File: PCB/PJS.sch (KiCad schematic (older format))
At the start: 40 parts, among them J1 HFW8R-1STE1H1LF_FFC, K1 G2R-2-DC5_Relay, Q1 MMBT222A_Transistor, X1 XT30-F_MotorConnector, X2 XT30-F_MotorConnector, X3 XT60-F_BatteryConnector

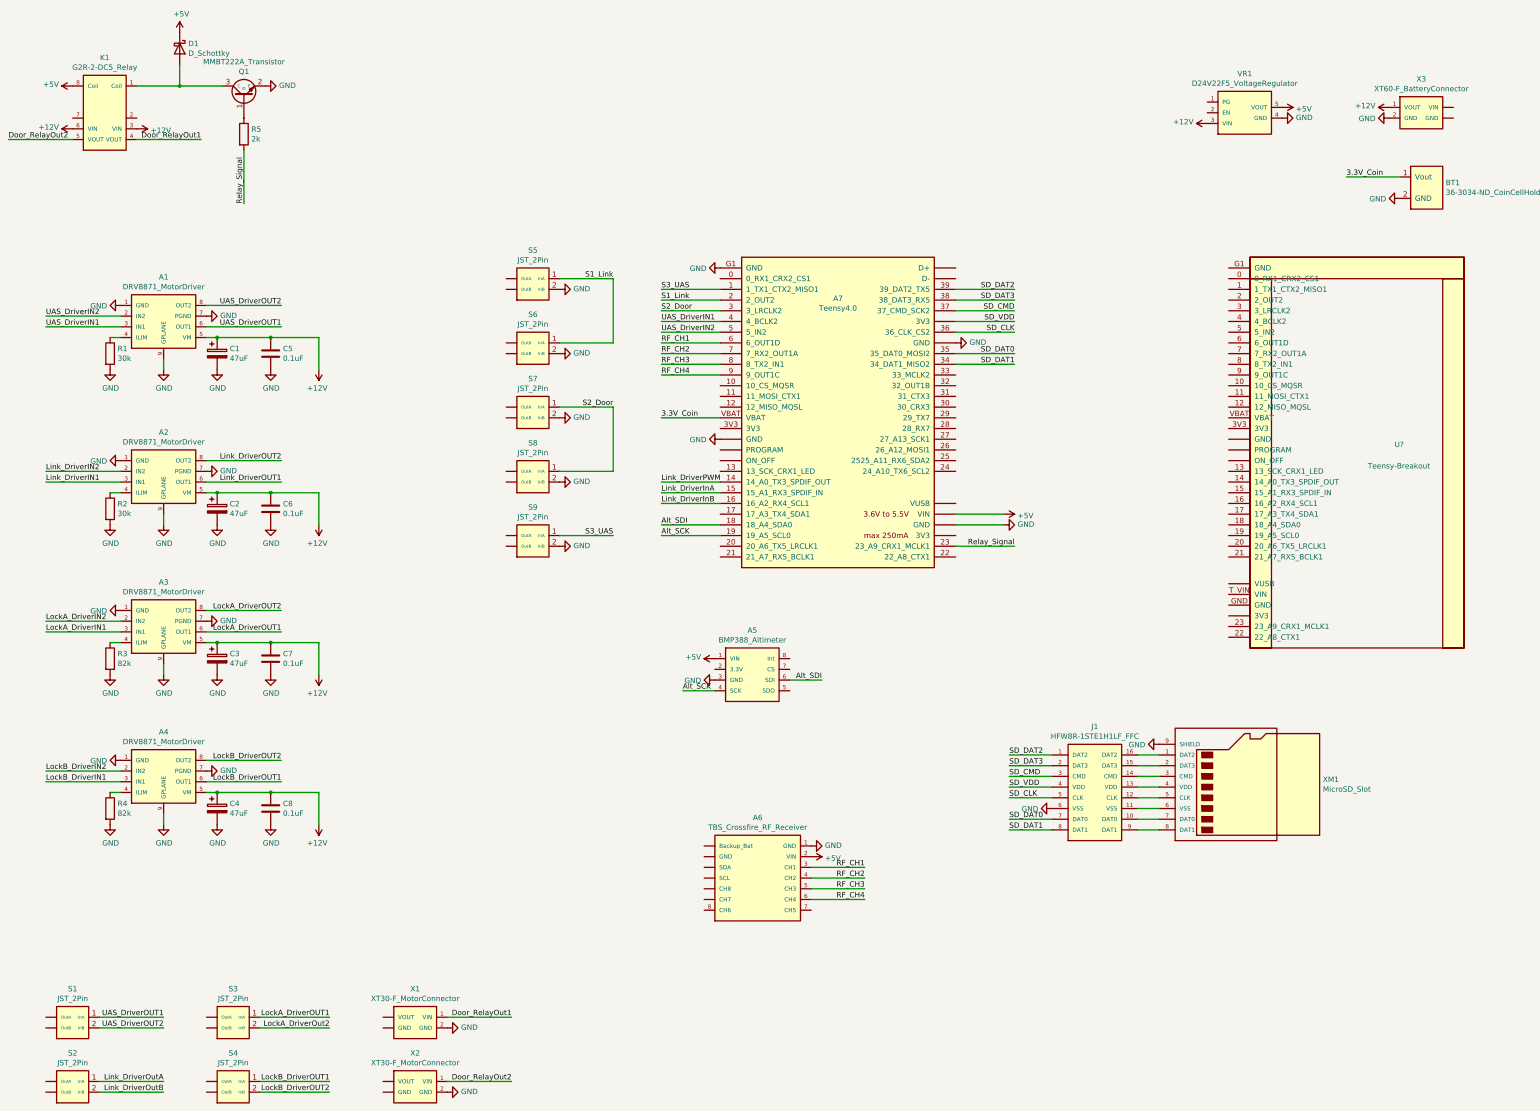
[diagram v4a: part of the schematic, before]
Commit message: 99.5% Complete Schematic and Footprint
The only item missing is the footprint for the RF receiver, which is now being mounted on the board.

Connectors for the motors and switches have now changed to two different locking JSTS.
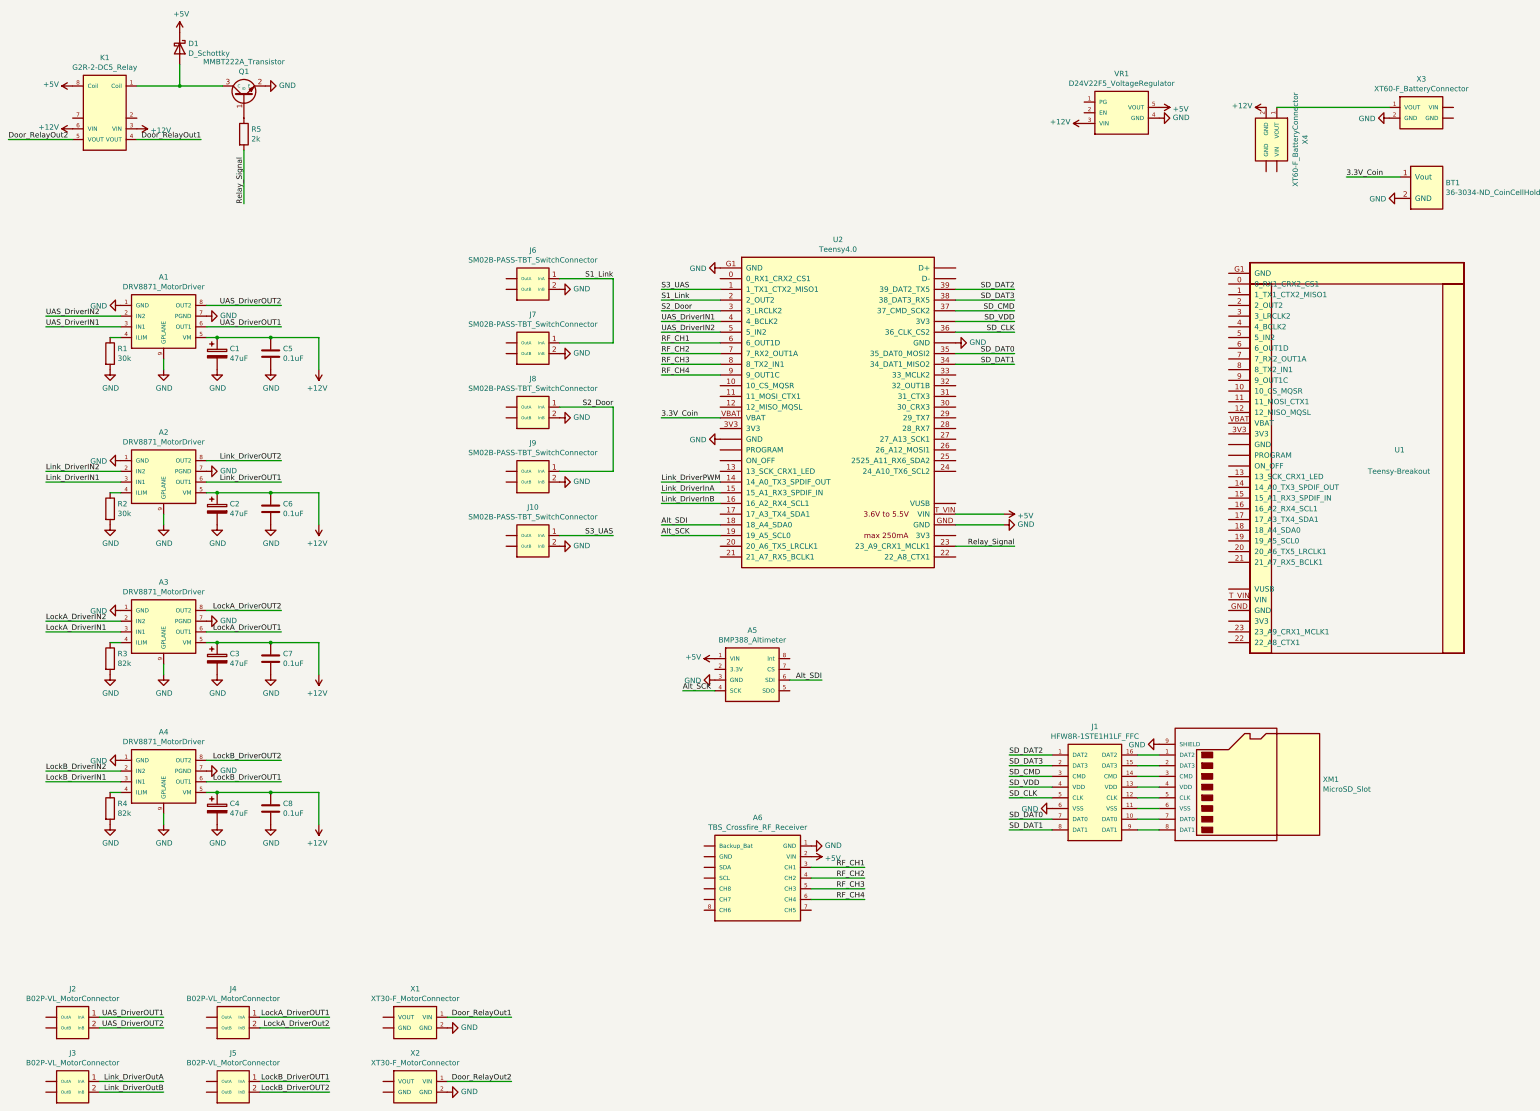
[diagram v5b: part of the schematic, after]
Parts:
- removed A7: Teensy4.0, PJS:Teensy4.0, symbol PJS-rescue:Teensy4.0-PJS
- removed S1, S2, S3, S4: JST_2Pin, PJS:JST_2Pin, symbol PJS:JST_2Pin
- removed S5, S6, S7, S8, S9: JST_2Pin, symbol PJS:JST_2Pin
- added J10, J6, J7, J8, J9: SM02B-PASS-TBT_SwitchConnector, PJS:SM02B-PASS-TBT_SwitchConnector, symbol PJS:SM02B-PASS-TBT_SwitchConnector
- added J2, J3, J4, J5: B02P-VL_MotorConnector, PJS:B02P-VL_MotorConnector, symbol PJS:B02P-VL_MotorConnector
- added U2: Teensy4.0, PJS:Teensy4.0, symbol PJS:Teensy4.0
- added X4: XT60-F_BatteryConnector, PJS:XT60_FemaleBatteryConnector, symbol PJS:XT60-F_BatteryConnector
- K1: footprint PJS:G2R-2-DC5 -> PJS:G2R-2-DC5_Relay
- R5: footprint PJS:MicroSD_Slot -> PJS:RMCF2512FT2K00_Resistor
- gave numbers to parts that had none: 1
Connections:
- net +12V: now also X4.2 (GND); no longer X3.1 (VOUT)
- net +5V: now also U2.T_VIN (VIN)
- net 3.3V_Coin: now also U2.VBAT
- net Alt_SCK: now also U2.19 (19_A5_SCL0)
- net Alt_SDI: now also U2.18 (18_A4_SDA0)
- net GND: now also J10.2 (InB), J6.2 (InB), J7.2 (InB), J8.2 (InB), J9.2 (InB), U2.G1 (GND), U2.GND, U2.~ (VUSB)
- net Link_DriverInA: now also U2.15 (15_A1_RX3_SPDIF_IN)
- net Link_DriverInB: now also U2.16 (16_A2_RX4_SCL1)
- net Link_DriverOutA: now also J3.1 (InA)
- net Link_DriverOutB: now also J3.2 (InB)
- net Link_DriverPWM: now also U2.14 (14_A0_TX3_SPDIF_OUT)
- net LockA_DriverOUT1: now also J4.1 (InA)
- net LockA_DriverOut2: now also J4.2 (InB)
- net LockB_DriverOUT1: now also J5.1 (InA)
- net LockB_DriverOUT2: now also J5.2 (InB)
- net RF_CH1: now also U2.6 (6_OUT1D)
- net RF_CH2: now also U2.7 (7_RX2_OUT1A)
- net RF_CH3: now also U2.8 (8_TX2_IN1)
- net RF_CH4: now also U2.9 (9_OUT1C)
- net Relay_Signal: now also U2.23 (23_A9_CRX1_MCLK1)
- net S1_Link: now also J6.1 (InA), J7.1 (InA), U2.2 (2_OUT2)
- net S2_Door: now also J8.1 (InA), J9.1 (InA), U2.3 (3_LRCLK2)
- net S3_UAS: now also J10.1 (InA), U2.1 (1_TX1_CTX2_MISO1)
- net SD_CLK: now also U2.36 (36_CLK_CS2)
- net SD_CMD: now also U2.37 (37_CMD_SCK2)
- net SD_DAT0: now also U2.35 (35_DAT0_MOSI2)
- net SD_DAT1: now also U2.34 (34_DAT1_MISO2)
- net SD_DAT2: now also U2.39 (39_DAT2_TX5)
- net SD_DAT3: now also U2.38 (38_DAT3_RX5)
- net SD_VDD: now also U2.~ (VUSB)
- net UAS_DriverIN1: now also U2.4 (4_BCLK2)
- net UAS_DriverIN2: now also U2.5 (5_IN2)
- net UAS_DriverOUT1: now also J2.1 (InA)
- net UAS_DriverOUT2: now also J2.2 (InB)
- new net: X3.1 (VOUT), X4.1 (VOUT)
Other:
- moved on the sheet: U1, VR1

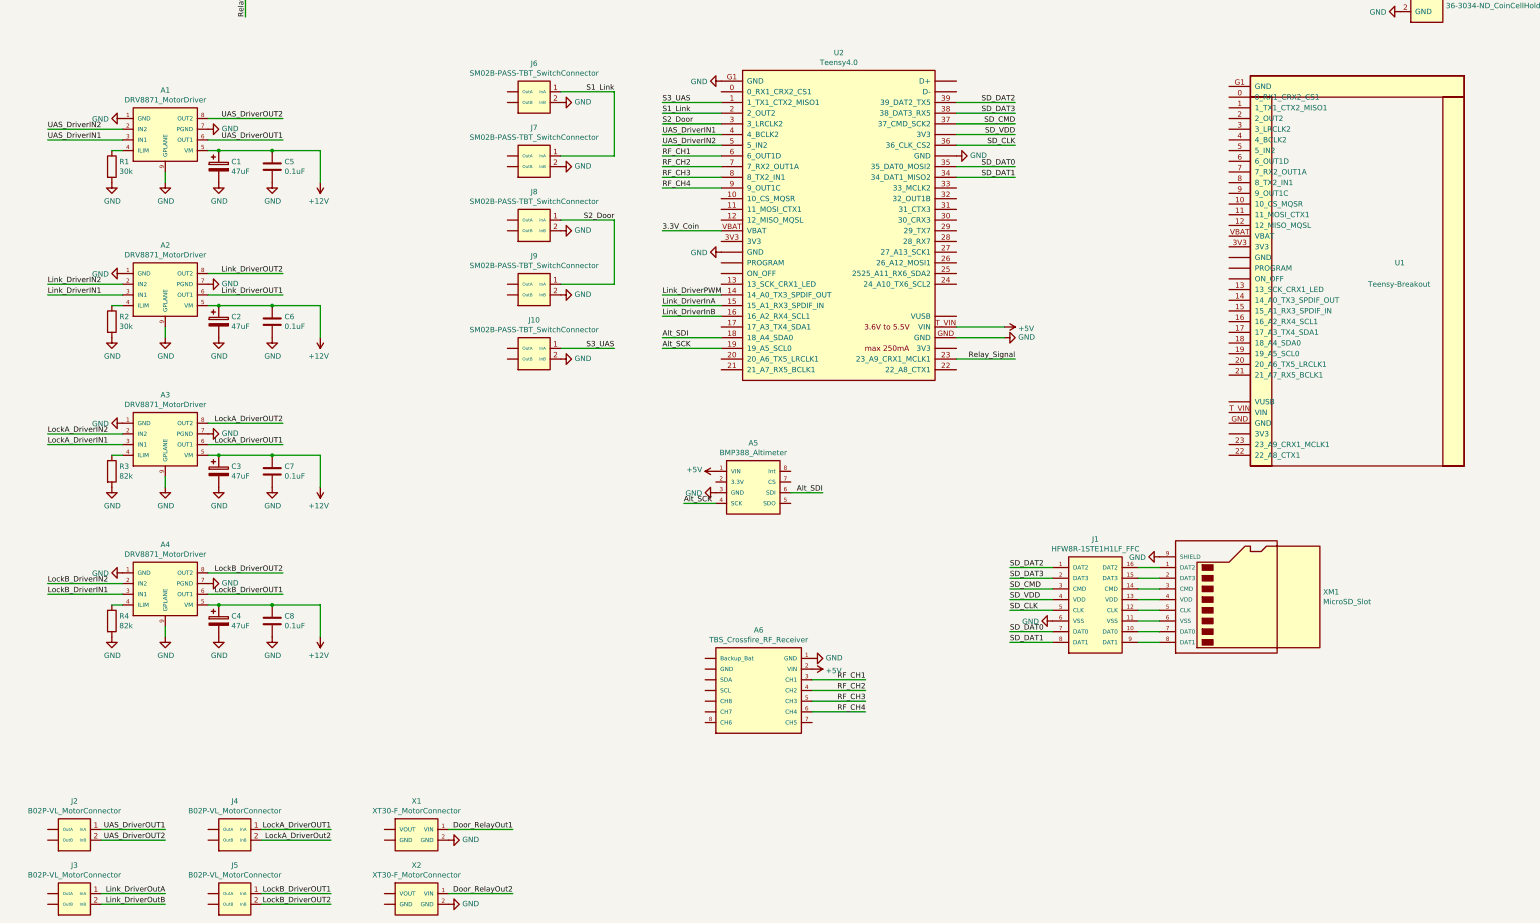
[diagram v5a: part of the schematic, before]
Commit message: Completed schematic and PCB layout
No components have .step files for rendering. The only footprint that is incorrect is the RF receiver, which is not yet mounted ion the board.
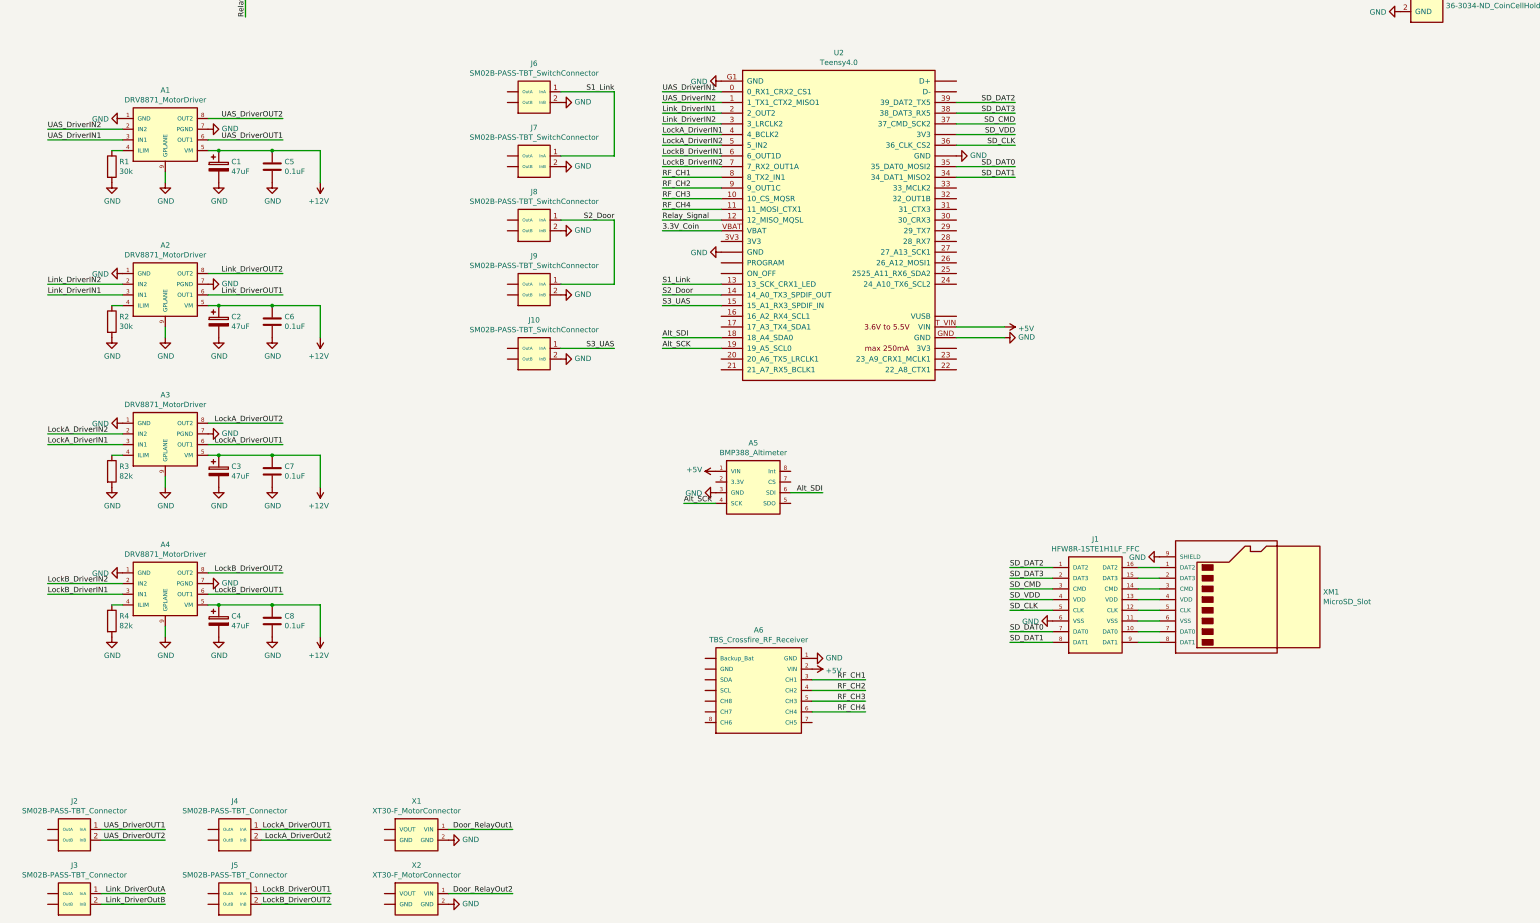
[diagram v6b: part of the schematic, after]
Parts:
- removed J2, J3, J4, J5: B02P-VL_MotorConnector, PJS:B02P-VL_MotorConnector, symbol PJS:B02P-VL_MotorConnector
- removed U1: Teensy-Breakout, PJS:Teensy4.0, symbol PJS:Teensy-Breakout
- added J2, J3, J4, J5: SM02B-PASS-TBT_Connector, PJS:SM02B-PASS-TBT_Connector, symbol PJS:SM02B-PASS-TBT_Connector
- J10, J6, J7, J8, J9: footprint PJS:SM02B-PASS-TBT_SwitchConnector -> PJS:SM02B-PASS-TBT_Connector
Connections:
- net Link_DriverInA is gone; now on net S3_UAS: U2.15 (15_A1_RX3_SPDIF_IN)
- net Link_DriverPWM is gone; now on net S2_Door: U2.14 (14_A0_TX3_SPDIF_OUT)
- net Link_DriverIN1: now also U2.2 (2_OUT2)
- net Link_DriverIN2: now also U2.3 (3_LRCLK2)
- net Link_DriverOutA: now also J3.1 (InA)
- net Link_DriverOutB: now also J3.2 (InB)
- net LockA_DriverIN1: now also U2.4 (4_BCLK2)
- net LockA_DriverIN2: now also U2.5 (5_IN2)
- net LockA_DriverOUT1: now also J4.1 (InA)
- net LockA_DriverOut2: now also J4.2 (InB)
- net LockB_DriverIN1: now also U2.6 (6_OUT1D)
- net LockB_DriverIN2: now also U2.7 (7_RX2_OUT1A)
- net LockB_DriverOUT1: now also J5.1 (InA)
- net LockB_DriverOUT2: now also J5.2 (InB)
- net RF_CH1: now also U2.8 (8_TX2_IN1); no longer U2.6 (6_OUT1D)
- net RF_CH2: now also U2.9 (9_OUT1C); no longer U2.7 (7_RX2_OUT1A)
- net RF_CH3: now also U2.10 (10_CS_MQSR); no longer U2.8 (8_TX2_IN1)
- net RF_CH4: now also U2.11 (11_MOSI_CTX1); no longer U2.9 (9_OUT1C)
- net Relay_Signal: now also U2.12 (12_MISO_MQSL); no longer U2.23 (23_A9_CRX1_MCLK1)
- net S1_Link: now also U2.13 (13_SCK_CRX1_LED); no longer U2.2 (2_OUT2)
- net S2_Door: no longer U2.3 (3_LRCLK2)
- net S3_UAS: no longer U2.1 (1_TX1_CTX2_MISO1)
- net UAS_DriverIN1: now also U2.0 (0_RX1_CRX2_CS1); no longer U2.4 (4_BCLK2)
- net UAS_DriverIN2: now also U2.1 (1_TX1_CTX2_MISO1); no longer U2.5 (5_IN2)
- net UAS_DriverOUT1: now also J2.1 (InA)
- net UAS_DriverOUT2: now also J2.2 (InB)
- net Link_DriverInB: no longer names the net of U2.16 (16_A2_RX4_SCL1)
